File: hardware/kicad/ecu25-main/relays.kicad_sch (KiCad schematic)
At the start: 32 parts, among them J15 Screw_Terminal_CONTACTOR, J8 Screw_Terminal_RELAY_OUT, K1 G5LE-1 24V, K2 G5LE-1 24V, K3 G5LE-1 24V, K4 G5LE-1 24V, K5 G5LE-1 24V, K6 G5LE-1 24V, Q60 2N7002K 60V, Q61 2N7002K 60V, Q62 2N7002K 60V, Q63 2N7002K 60V, Q64 2N7002K 60V, Q65 2N7002K 60V

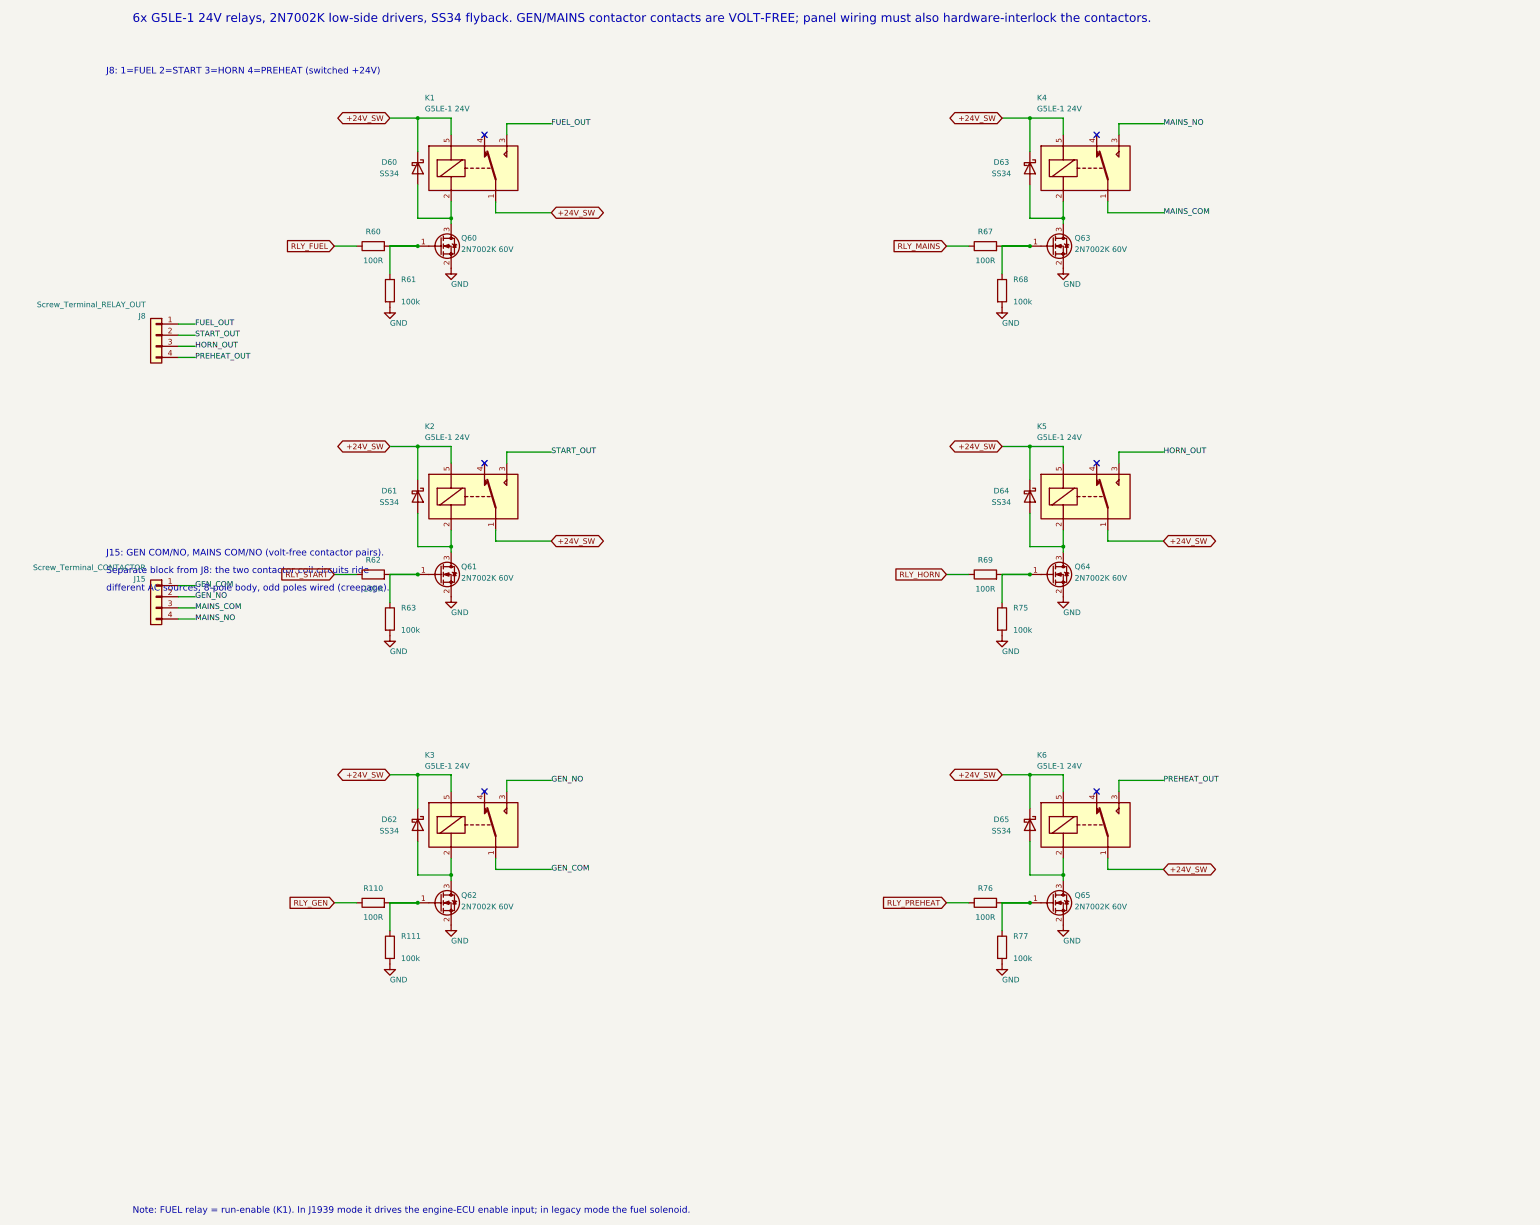
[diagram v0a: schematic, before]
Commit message: Convert hardware to 12 V system; pilot-duty output stage
The target set is a Kirloskar KG4-25WS1 (engine 3R550ETA 4G1, CPCB IV+):
12 V electrical system, 75 Ah battery, 3-cylinder CRDi with EGR + DOC.
The board was designed 24 V throughout, which was wrong.

Power:
- Rails renamed +24V/+24V_SW -> +12V/+12V_SW
- Buck UVLO 8.0 V -> 6.5 V (R3 30.1k), RON 100k -> 49.9k to hold ~300 kHz
  from a 12 V input
- New D3 blocking Schottky + C9 2200uF hold-up on the buck input. UVLO now
  senses the hold-up node, not the battery: sensing the battery would trip EN
  the moment the harness sagged during crank and switch the buck off while C9
  still held charge. Sized for >50 ms down to 6.5 V with the backlight shed
- Input protection rescaled for 12 V: D1 SMCJ33CA -> SMCJ16CA (clamps ~26 V
  not 53 V), D80 -> SMBJ16CA, D2 gate zener 15 V -> 12 V, C1 63 V -> 35 V

Outputs — the board no longer sources any field current:
- J8 becomes a 6-pole body with 5 poles wired: pin 1 OUT_COM is the common
  contact supply, fed by the INSTALLER from a fused source. Relay contact COMs
  come from it, not from the board rail
- +12V_SW now feeds only the six relay coils (200 mA) and D+ (100 mA)
- START marked pilot-only: a 12 V starter solenoid pulls 20-40 A and glow
  plugs 28-60 A, against 8 A DC contacts
- K5/K6 HORN/PREHEAT -> configurable AUX1/AUX2; on a CRDi engine the ECU owns
  the cold-start aid, so a fixed preheat channel would often go unused
- Relay coils G5LE-1-DC24 -> DC12 (360 ohm / 33 mA)

Analog rescaled for 12 V:
- DIN dividers 10k/3.3k -> 5.6k/1.8k, restoring 1.6 mA contact wetting
  (10k/3.3k gives only 0.9 mA at 12 V), debounce cap 470 nF -> 1 uF
- Battery and D+ sense 100k/6.8k -> 100k/22k, so 16 V uses most of the ADC span
- D+ excitation 220R 5W -> 120R 3W for the same 100 mA at 12 V

Verified: netlist sweep clean, no courtyard overlaps, nothing outside the
outline, DRC reports no errors (unrouted ratsnest and silk warnings aside).
Docs and firmware follow in the next com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
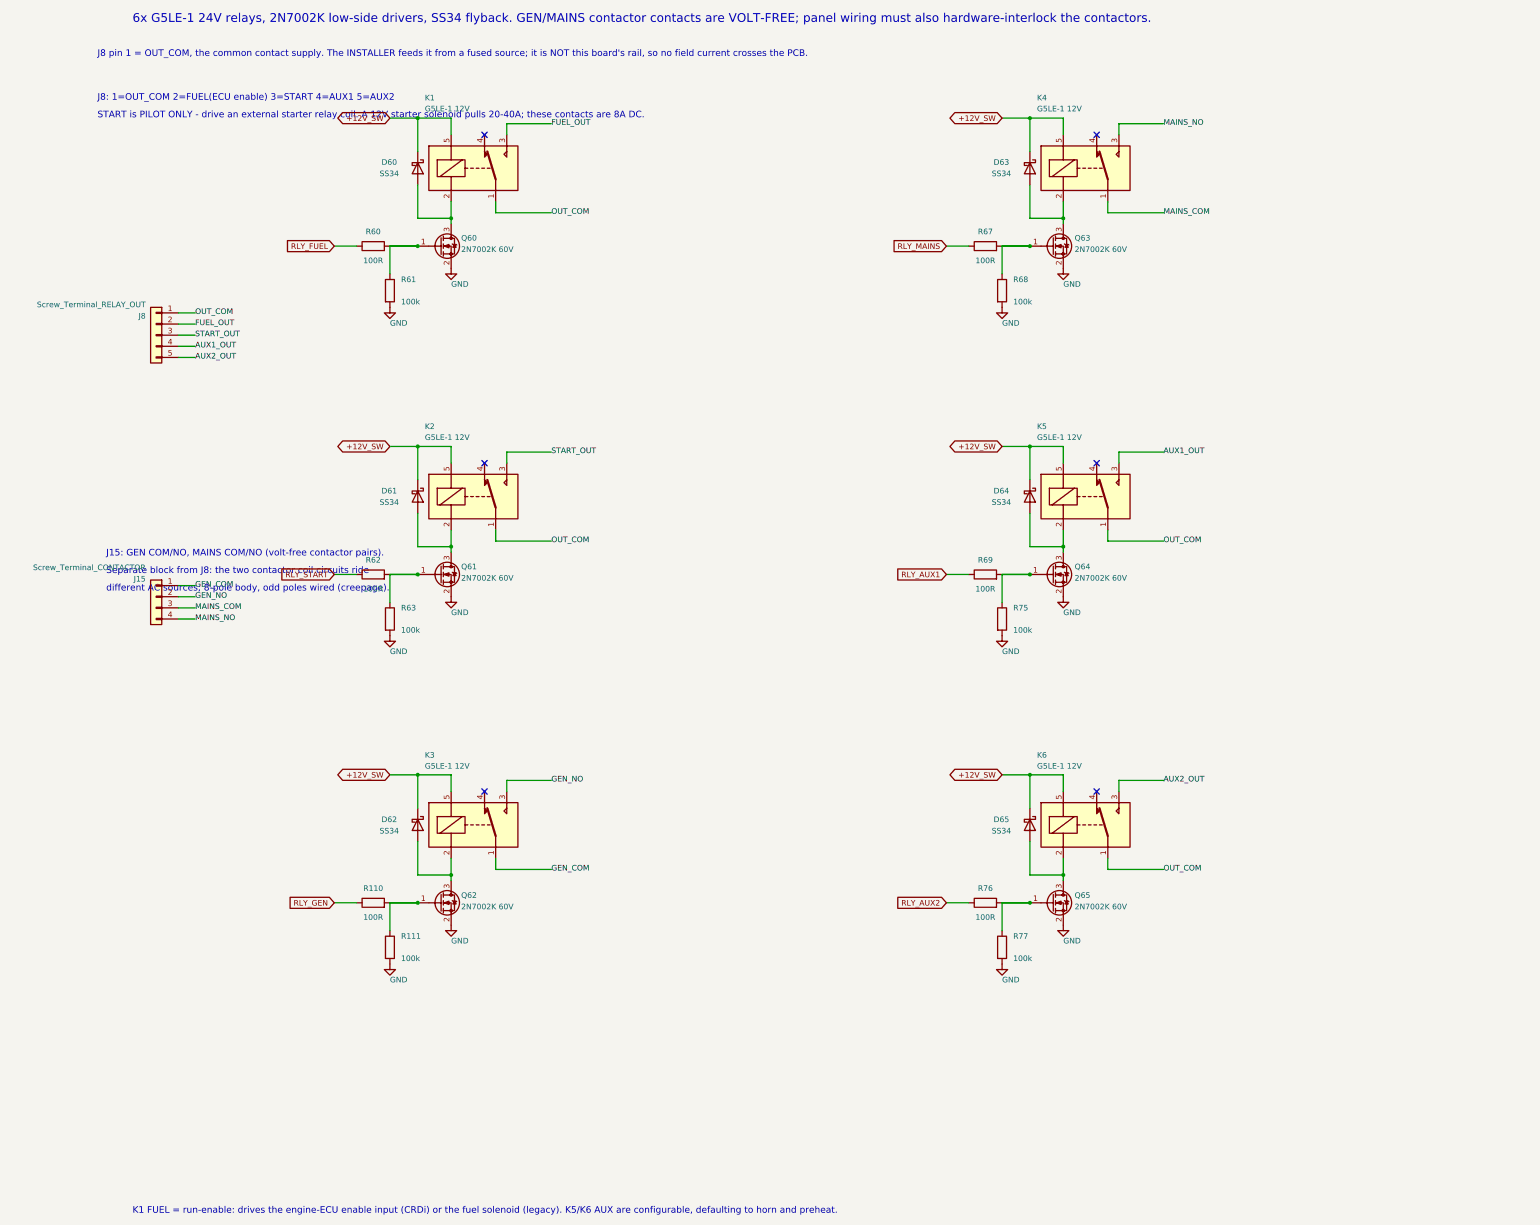
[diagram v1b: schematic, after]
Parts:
- removed J8: Screw_Terminal_RELAY_OUT, TerminalBlock_Phoenix:TerminalBlock_Phoenix_MKDS-3-4-5.08_1x04_P5.08mm_Horizontal, symbol Connector_Generic:Conn_01x04
- added J8: Screw_Terminal_RELAY_OUT, TerminalBlock_Phoenix:TerminalBlock_Phoenix_MKDS-3-6-5.08_1x06_P5.08mm_Horizontal, symbol Connector_Generic:Conn_01x05
- K1, K2, K3, K4, K5, K6: value G5LE-1 24V -> G5LE-1 12V
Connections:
- net FUEL_OUT: now also J8.2 (Pin_2)
- net START_OUT: now also J8.3 (Pin_3)
- net +24V_SW renamed +12V_SW
- net +12V_SW: no longer K1.1, K2.1, K5.1, K6.1
- net HORN_OUT renamed AUX1_OUT
- net AUX1_OUT: now also J8.4 (Pin_4)
- net PREHEAT_OUT renamed AUX2_OUT
- net AUX2_OUT: now also J8.5 (Pin_5)
- net RLY_HORN renamed RLY_AUX1
- net RLY_PREHEAT renamed RLY_AUX2
- new net OUT_COM: J8.1 (Pin_1), K1.1, K2.1, K5.1, K6.1
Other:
- note added: "J8 pin 1 = OUT_COM, the common contact supply. The INSTALLER feeds it from a fused source; it is NOT this board's rail, so no field current crosses the PCB."
- note added: "J8: 1=OUT_COM 2=FUEL(ECU enable) 3=START 4=AUX1 5=AUX2"
- note added: "K1 FUEL = run-enable: drives the engine-ECU enable input (CRDi) or the fuel solenoid (legacy). K5/K6 AUX are configurable, defaulting to horn and preheat."
- note added: "START is PILOT ONLY - drive an external starter relay coil. A 12V starter solenoid pulls 20-40A; these contacts are 8A DC."
- note removed: "J8: 1=FUEL 2=START 3=HORN 4=PREHEAT (switched +24V)"
- note removed: "Note: FUEL relay = run-enable (K1). In J1939 mode it drives the engine-ECU enable input; in legacy mode the fuel solenoid."

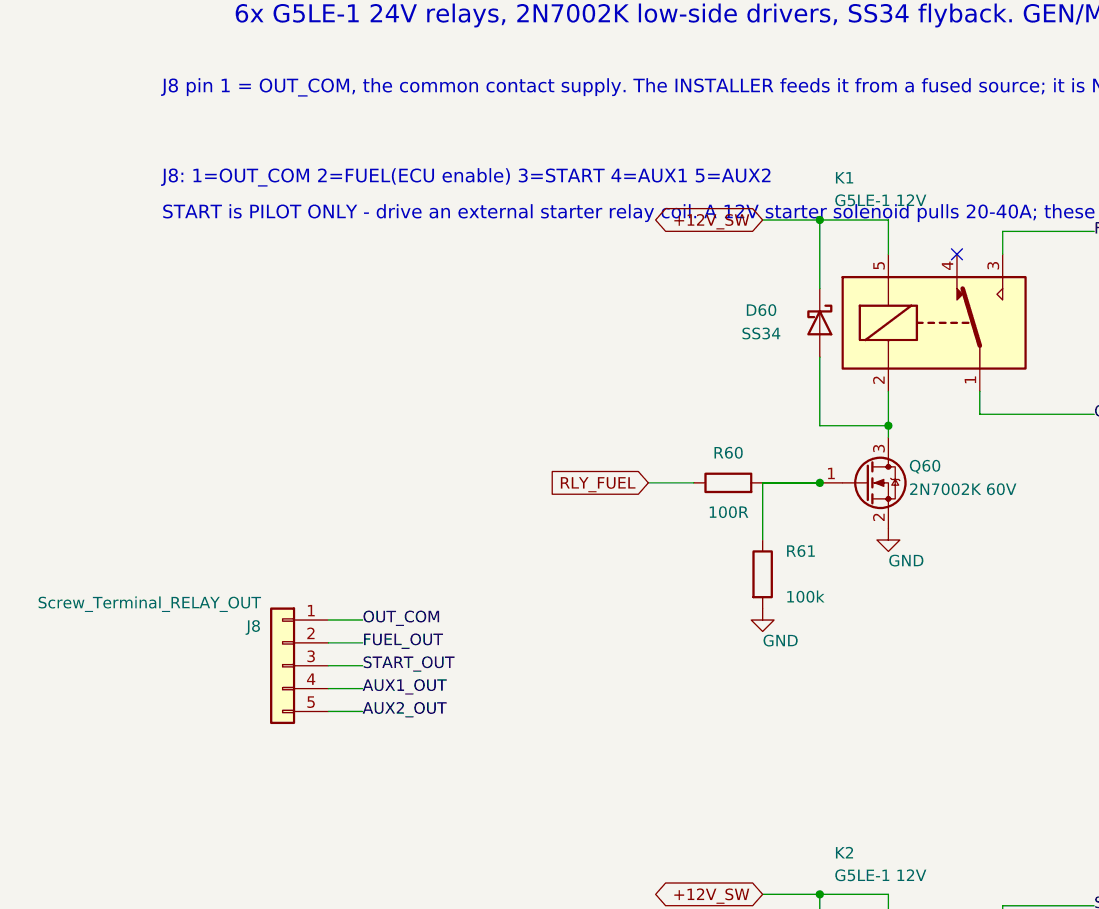
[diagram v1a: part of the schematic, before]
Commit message: Fix SME review findings on the 12 V conversion
Two criticals, both of which would have reached a real installation:

- gcu_config.c still carried 24 V battery thresholds (22 V low / 30 V high).
  On a 12 V set batt_low was permanently true, so 60 s after every power-up
  the alarm latched and pinned the horn relay on for good — while batt_high
  at 30 V could never trip, leaving a runaway regulator undetected exactly
  where the new 16 V TVS starts conducting. Now 11.0 / 15.5 V, with a
  regression test that runs 90 s at 13.8 V and asserts silence
- docs/ecu-25-explained.md still told the installer to wire the starter
  solenoid straight to K2 at '16 A'. A G5LE-1 is 8 A DC and a 12 V starter
  solenoid pulls 20-40 A: the contacts weld, and a welded starter contact
  means the engine cranks and cannot be commanded to stop. Section rewritten
  around the dry-contact stage

Majors:
- gen_pcb.py netclass patterns still named +24V/+24V_SW, so the battery rail,
  the switched rail, the hold-up node and OUT_COM all fell through to a
  0.25 mm Default track — OUT_COM being the common return for every field
  contact. Fixed, and the generator now fails if any netclass pattern matches
  no net, which is what would have caught it
- DIN ground-side pull-up 5.6k -> 2.2k: at 5.6k an open contact sat at 1.66 V,
  inside the STM32's indeterminate band (V_IL 1.12 / V_IH 1.79)
- Buck RON 49.9k -> 41.2k. The LM5164's f_SW = V_OUT x 2500 / R_RON has no
  V_IN term — on-time varies inversely with V_IN precisely so frequency stays
  constant — so the rationale in two documents was wrong, and the original
  100k was never 300 kHz at any input voltage, it was 125 kHz
- modbus_rx guarded resp_max >= 5 but the FC06/FC16 echo paths write 8 bytes,
  running three bytes past the caller's buffer. Guard raised to 8
- Modbus no longer publishes a fabricated power factor: registers 19/20 now
  carry real_power_w and power_factor from gcu_inputs_t, which the AC layer
  fills. A constant 0.800 in a S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
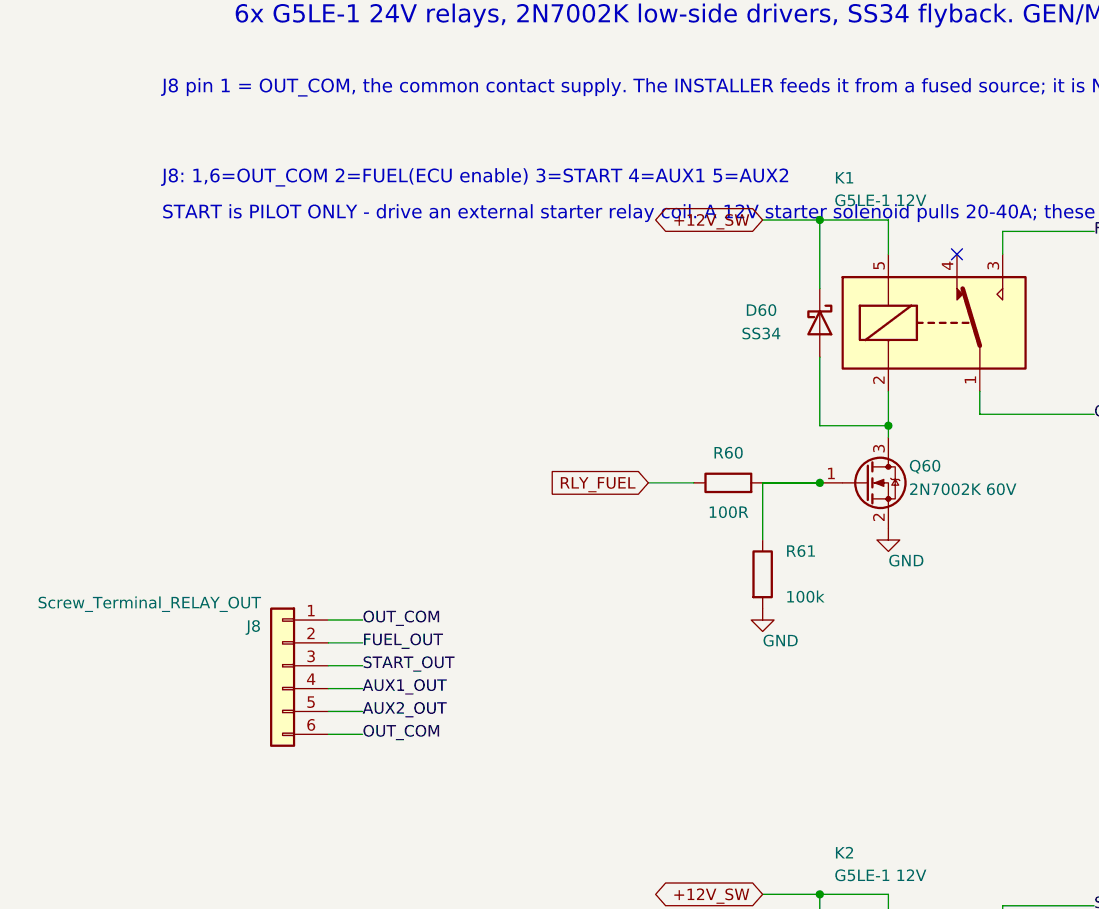
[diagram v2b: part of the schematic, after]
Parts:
- removed J8: Screw_Terminal_RELAY_OUT, TerminalBlock_Phoenix:TerminalBlock_Phoenix_MKDS-3-6-5.08_1x06_P5.08mm_Horizontal, symbol Connector_Generic:Conn_01x05
- added J8: Screw_Terminal_RELAY_OUT, TerminalBlock_Phoenix:TerminalBlock_Phoenix_MKDS-3-6-5.08_1x06_P5.08mm_Horizontal, symbol Connector_Generic:Conn_01x06
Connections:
- net AUX1_OUT: now also J8.4 (Pin_4)
- net AUX2_OUT: now also J8.5 (Pin_5)
- net FUEL_OUT: now also J8.2 (Pin_2)
- net OUT_COM: now also J8.1 (Pin_1), J8.6 (Pin_6)
- net START_OUT: now also J8.3 (Pin_3)
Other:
- note added: "J8: 1,6=OUT_COM 2=FUEL(ECU enable) 3=START 4=AUX1 5=AUX2"
- note removed: "J8: 1=OUT_COM 2=FUEL(ECU enable) 3=START 4=AUX1 5=AUX2"

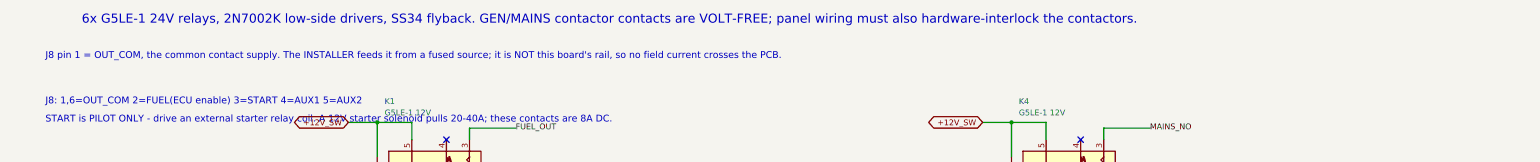
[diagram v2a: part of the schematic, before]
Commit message: Fix SME verification findings; add COT ripple injection and the I/O map
An independent verification pass re-derived the 12 V conversion fixes against
the TI, Omron, Nexperia and ST datasheets instead of trusting the commit
message. The hold-up energy math, the RON/UVLO arithmetic, the modbus_rx
bounds, the AUX refactor and the dry-contact output stage all held. Eleven
majors did not.

Hardware:
- The buck had no ripple-injection network. The LM5164 is constant-on-time:
  it restarts the on-time when FB falls to the 1.2 V reference, so it needs
  >=20 mV of FB ripple IN PHASE with the inductor current. Two 22 uF ceramics
  give 2.7 mV, and that component is capacitive, i.e. out of phase — the
  required series ESR would be 0.287 ohm against the ~2 mohm they actually
  have. The part would have burst-switched: several on-times in close
  succession then a long off-time. Added the datasheet's Type-3 network
  (R7 100k, C10 4.7nF, C11 1nF C0G), which builds the ramp from SW and
  couples it into FB, leaving output ripple untouched. 21 mV at 12.6 V in,
  13 mV at 8 V, against a 12 mV floor
- DIN ground-side pull-up 2.2k -> 1k. 2.2k sat at 2.25 V at 12.6 V but fell
  to 1.59 V during an 8.5 V crank sag — back inside the STM32's indeterminate
  band. The value has to be set by the worst case: V_bat x 1.8/(R+7.4) needs
  R <= 670 ohm to clear V_IH 1.785 V at 8.0 V
- The hold-up node was still the autogenerated Net-(D3-K), so the netclass
  rule and the DRU keyed off a reference designator. Now labelled +12V_HLD
- C9 25 V -> 35 V never reached the orderable BOM: gen_bom.py still said
  "2200 uF 25 V radial" for a node the design puts at 25.6 V
- OUT_COM moved to the Battery class and given a stated ceiling: 4 A total,
  2 A per output, installer fuse 4 A. Four 8 A contacts on a trunk sized for
  4 A needed writing down; it was implied by the netclass and nowhere else
- gen_pcb.py netclass assertion rewritten. It was blind to exactly the
  suffix patterns it was written to pr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
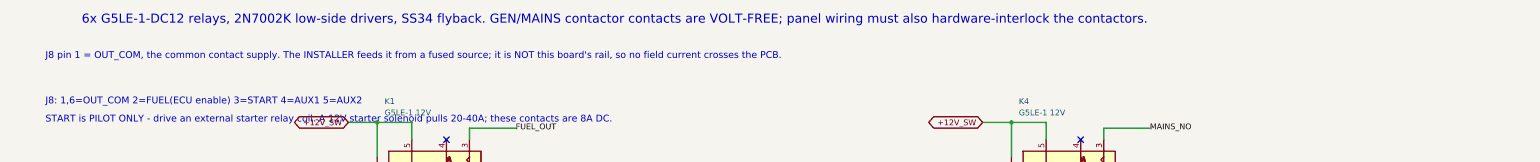
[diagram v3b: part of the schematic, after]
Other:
- note added: "6x G5LE-1-DC12 relays, 2N7002K low-side drivers, SS34 flyback. GEN/MAINS contactor contacts are VOLT-FREE; panel wiring must also hardware-interlock the contactors."
- note removed: "6x G5LE-1 24V relays, 2N7002K low-side drivers, SS34 flyback. GEN/MAINS contactor contacts are VOLT-FREE; panel wiring must also hardware-interlock the contactors."
